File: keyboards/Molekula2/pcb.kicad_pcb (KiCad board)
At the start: 2 copper layers, 276 x 87.2 mm, 93 parts, among them J1 N!N, J10 Conn_01x12_Socket, J11 Conn_01x12_Socket, J12 Conn_01x02_Socket, J2 C479750, J3 C479750, J4 C479750, J5 C479750, J6 Display_nice-view, J7 Conn_01x02_Socket, J8 C262499, J9 C262499, SW1 Switch, SW10 Switch, SW11 Switch, SW12 Switch, SW13 Switch, SW14 Switch, SW15 Switch, SW16 Switch, SW17 Switch, SW18 Switch, SW19 Switch, SW2 Switch, SW20 Switch, SW21 Switch, SW22 Switch, SW23 Switch, SW24 Switch, SW25 Switch, SW26 Switch, SW27 Switch, SW28 Switch, SW29 Switch, SW3 Switch, SW30 Switch, SW31 Switch, SW32 Switch, SW33 Switch, SW34 Switch, SW35 Switch, SW36 Switch, SW37 SW_Push, SW38 RotaryEncoder_Switch, SW4 Switch, SW5 Switch, SW6 Switch, SW7 Switch, SW8 Switch, SW9 Switch

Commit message: feat: add 2 more keys to the upper row and updated bom
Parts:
- added D37: C81598, zzkeeb:Diode_1N4148-SOD123, B.Cu at (80.9, 68.7)
- added D38: C81598, zzkeeb:Diode_1N4148-SOD123, B.Cu at (318.9, 68.7)
- added SW39: Switch, zzkeeb:Switch_MXKSChoc-miny-hotswap-chocv2-3d, F.Cu at (71.4, 71.0)
- added SW40: Switch, zzkeeb:Switch_MXKSChoc-miny-hotswap-chocv2-3d, F.Cu at (328.4, 71.0)
- moved SW1 24.8 mm to (90.4, 55.0)
- moved SW23 24.8 mm to (309.4, 55.0)
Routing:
- net row7: track 31.5 -> 179.6 mm, vias 2 -> 3
- net row3: track 38.7 -> 182.5 mm, vias 2 -> 3
- net Net-(D38-A): track 0.00 -> 28.8 mm
- net Net-(D1-A): track 121.7 -> 96.2 mm
- net Net-(D23-A): track 135.4 -> 114.5 mm
- net col9: track 138.2 -> 145.6 mm, vias 3 -> 4
- net Net-(D37-A): track 0.00 -> 7.37 mm
- net col0: track 161.0 -> 168.0 mm
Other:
- board size 276 x 87.2 mm -> 276.5 x 87.2 mm
- board text added: "github.com/ opendata-nuernberg/molekula"
- board text added: "v1.0"
- board text removed: "github.com/zzeneg/molekula"

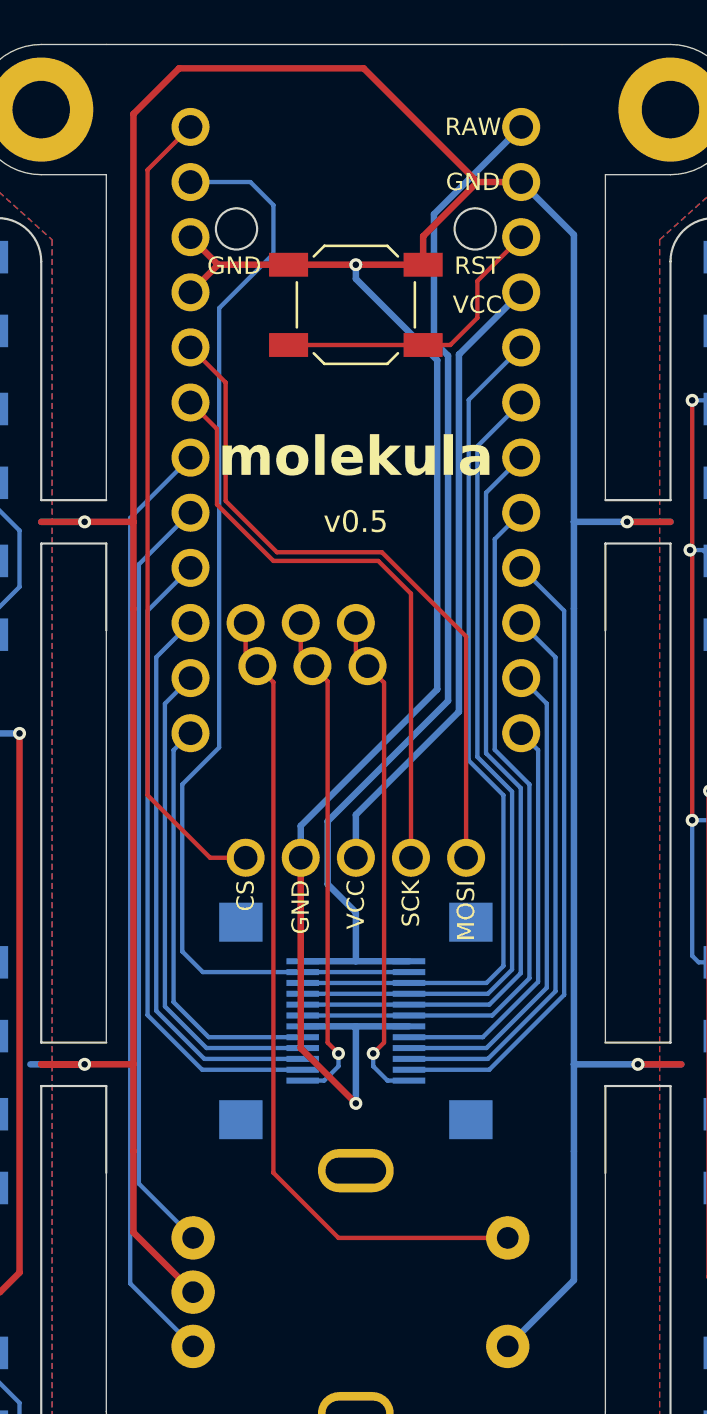
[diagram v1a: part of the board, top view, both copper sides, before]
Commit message: feat: change MCU to RP2040
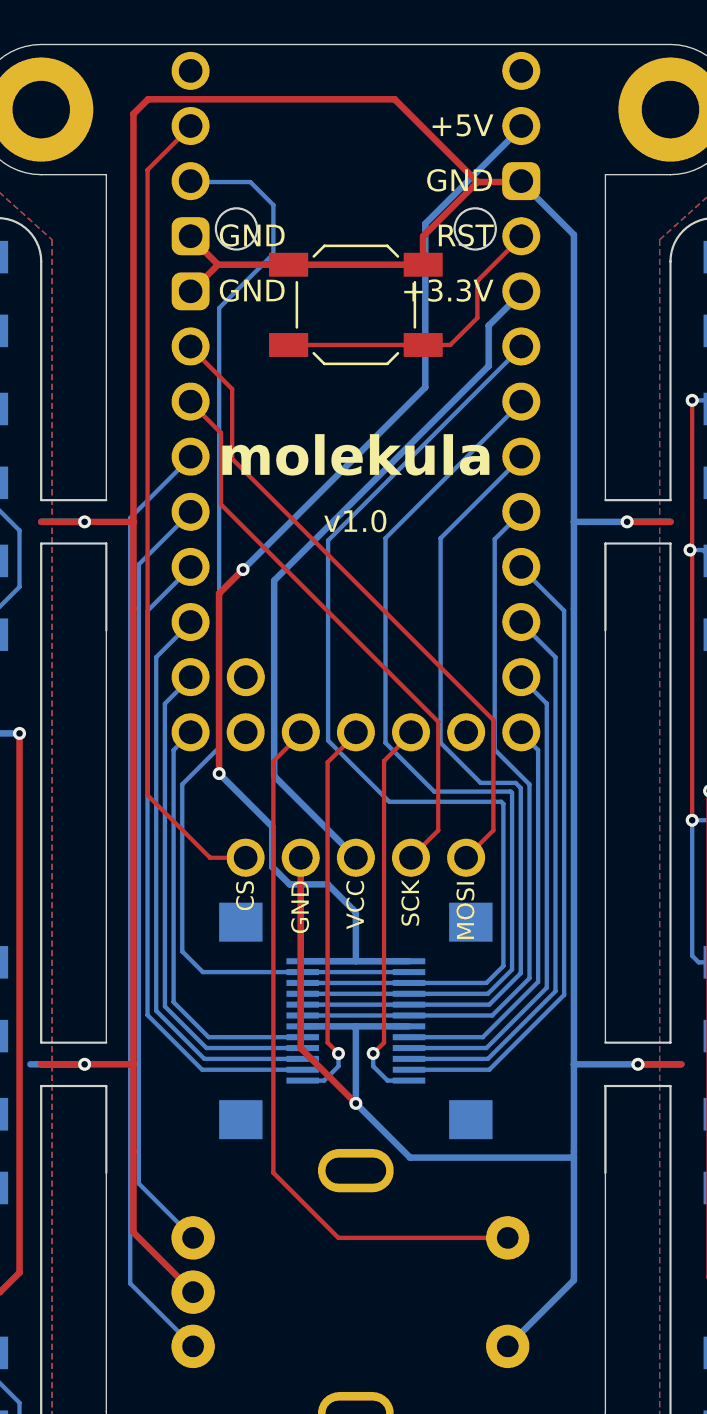
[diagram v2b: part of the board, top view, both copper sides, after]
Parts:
- removed J1: N!N, zzkeeb:MCU_nice-nano
- added J13: RP2040, zzkeeb:MCU_rp2040-helios, F.Cu at (199.9, 54.7)
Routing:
- net GND: track 358.6 -> 337.1 mm, vias 11 -> 10
- net col3-mcu: track 39.7 -> 48.1 mm
- net col2-mcu: track 37.7 -> 43.3 mm
- net free1-mcu: track 23.1 -> 18.1 mm
- net OFF: track 37.9 -> 32.9 mm
- net free2-mcu: track 23.1 -> 18.1 mm
- net BAT-mcu: track 48.1 -> 52.8 mm, vias 0 -> 2
- net +3.3V: track 29.2 -> 32.4 mm
- net col1-mcu: track 35.7 -> 38.4 mm
- net MOSI: track 31.6 -> 29.8 mm
- net SCK: track 28.0 -> 26.2 mm
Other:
- board text removed: "v0.5"
